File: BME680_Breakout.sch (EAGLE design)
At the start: 8 parts, among them U1 BME680

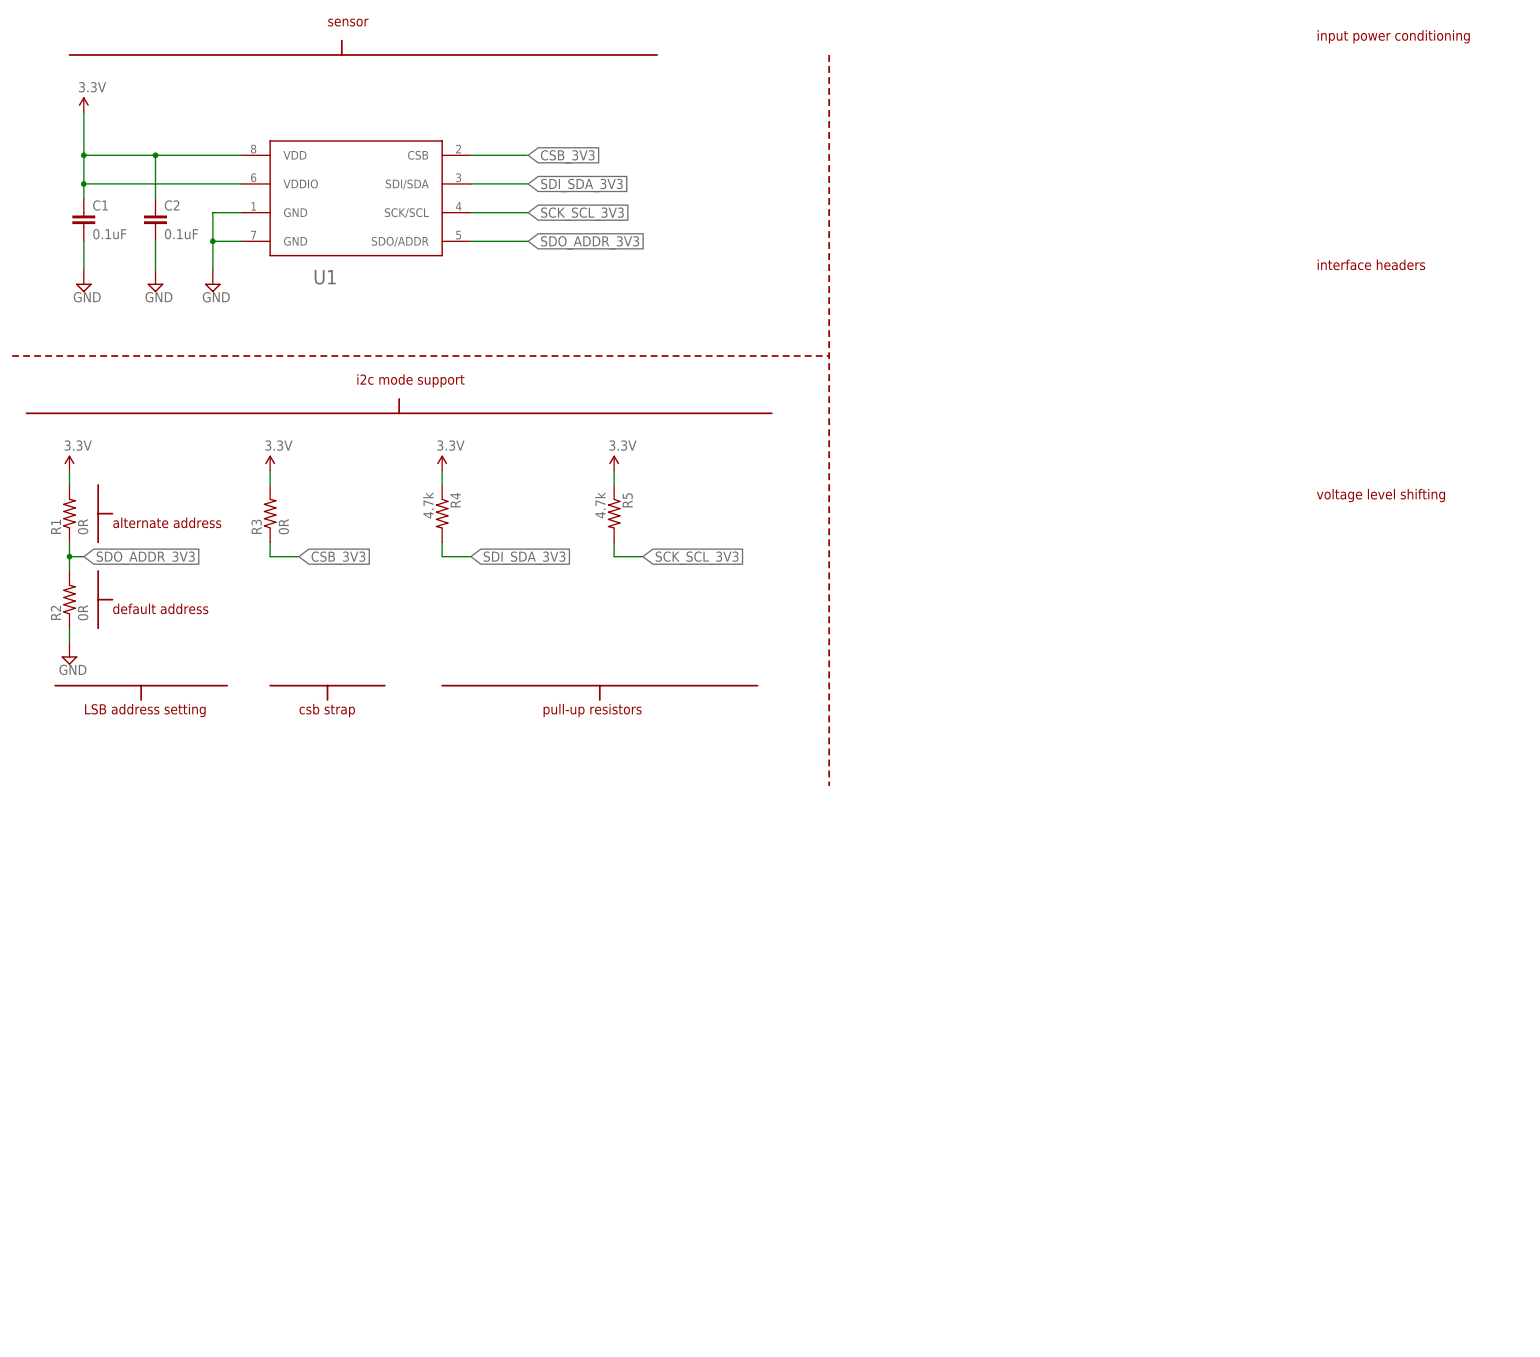
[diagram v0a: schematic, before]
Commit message: settled on i2c, renamed some signals, added level shifter logic
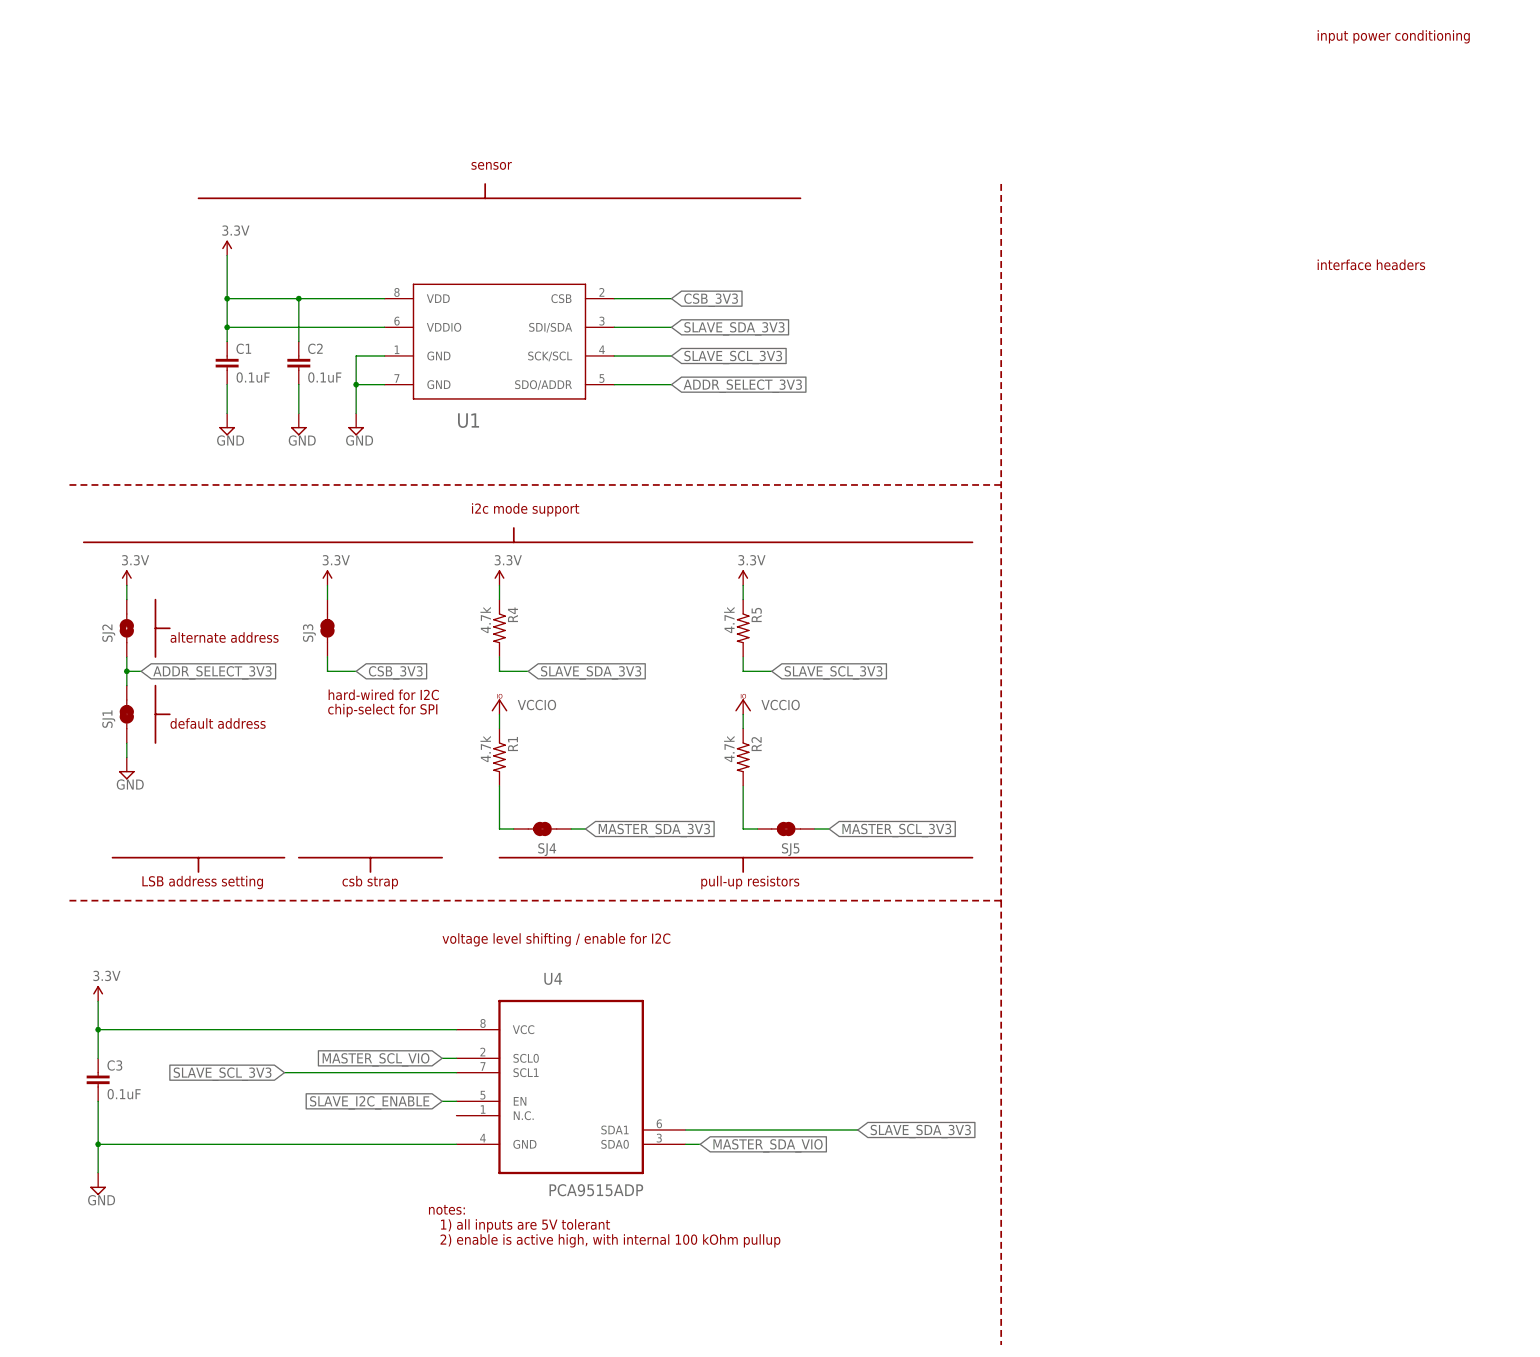
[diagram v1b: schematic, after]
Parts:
- removed R3: 0R, SparkFun-Passives:RESISTOR0805-RES
- added C3: 0.1uF, SparkFun-Passives:CAP0805
- added SJ1, SJ3, SJ4, SJ5: JUMPER-PAD-2-NC_BY_TRACE, SparkFun-Passives:JUMPER-PAD-2-NC_BY_TRACE
- added SJ2: JUMPER-PAD-2-NOYES_SILK, SparkFun-Passives:JUMPER-PAD-2-NOYES_SILK
- added U4: PCA9515ADP, PCA9515ADP:PCA9515ADP
- R1, R2: value 0R -> 4.7k
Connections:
- removed net SCK_SCL_3V3: R5.2, U1.SCK/SCL
- removed net SDI_SDA_3V3: R4.2, U1.SDI/SDA
- removed net SDO_ADDR_3V3: R1.1, R2.2, U1.SDO/ADDR
- new net ADDR_SELECT_3V3: SJ1.2, SJ2.1, U1.SDO/ADDR
- new net MASTER_SCL_3V3: SJ5.1
- new net MASTER_SCL_VIO: U4.SCL0
- new net MASTER_SDA_3V3: SJ4.1
- new net MASTER_SDA_VIO: U4.SDA0
- new net N$1: R1.2, SJ4.2
- new net N$2: R2.2, SJ5.2
- new net SLAVE_I2C_ENABLE: U4.EN
- new net SLAVE_SCL_3V3: R5.2, U1.SCK/SCL, U4.SCL1
- new net SLAVE_SDA_3V3: R4.2, U1.SDI/SDA, U4.SDA1
- new net VCCIO: R1.1, R2.1
- net 3.3V: now also C3.1, SJ2.2, SJ3.2, U4.VCC; no longer R1.2, R3.2
- net CSB_3V3: now also SJ3.1; no longer R3.1
- net GND: now also C3.2, SJ1.1, U4.GND; no longer R2.1
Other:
- note added: "chip-select for SPI"
- note added: "hard-wired for I2C"
- note added: "notes: 1) all inputs are 5V tolerant 2) enable is active high, with internal 100 kOhm pullup"
- note added: "voltage level shifting / enable for I2C"
- note removed: "voltage level shifting"
- moved on the sheet: C1, C2, R1, R2, R4, R5, U1

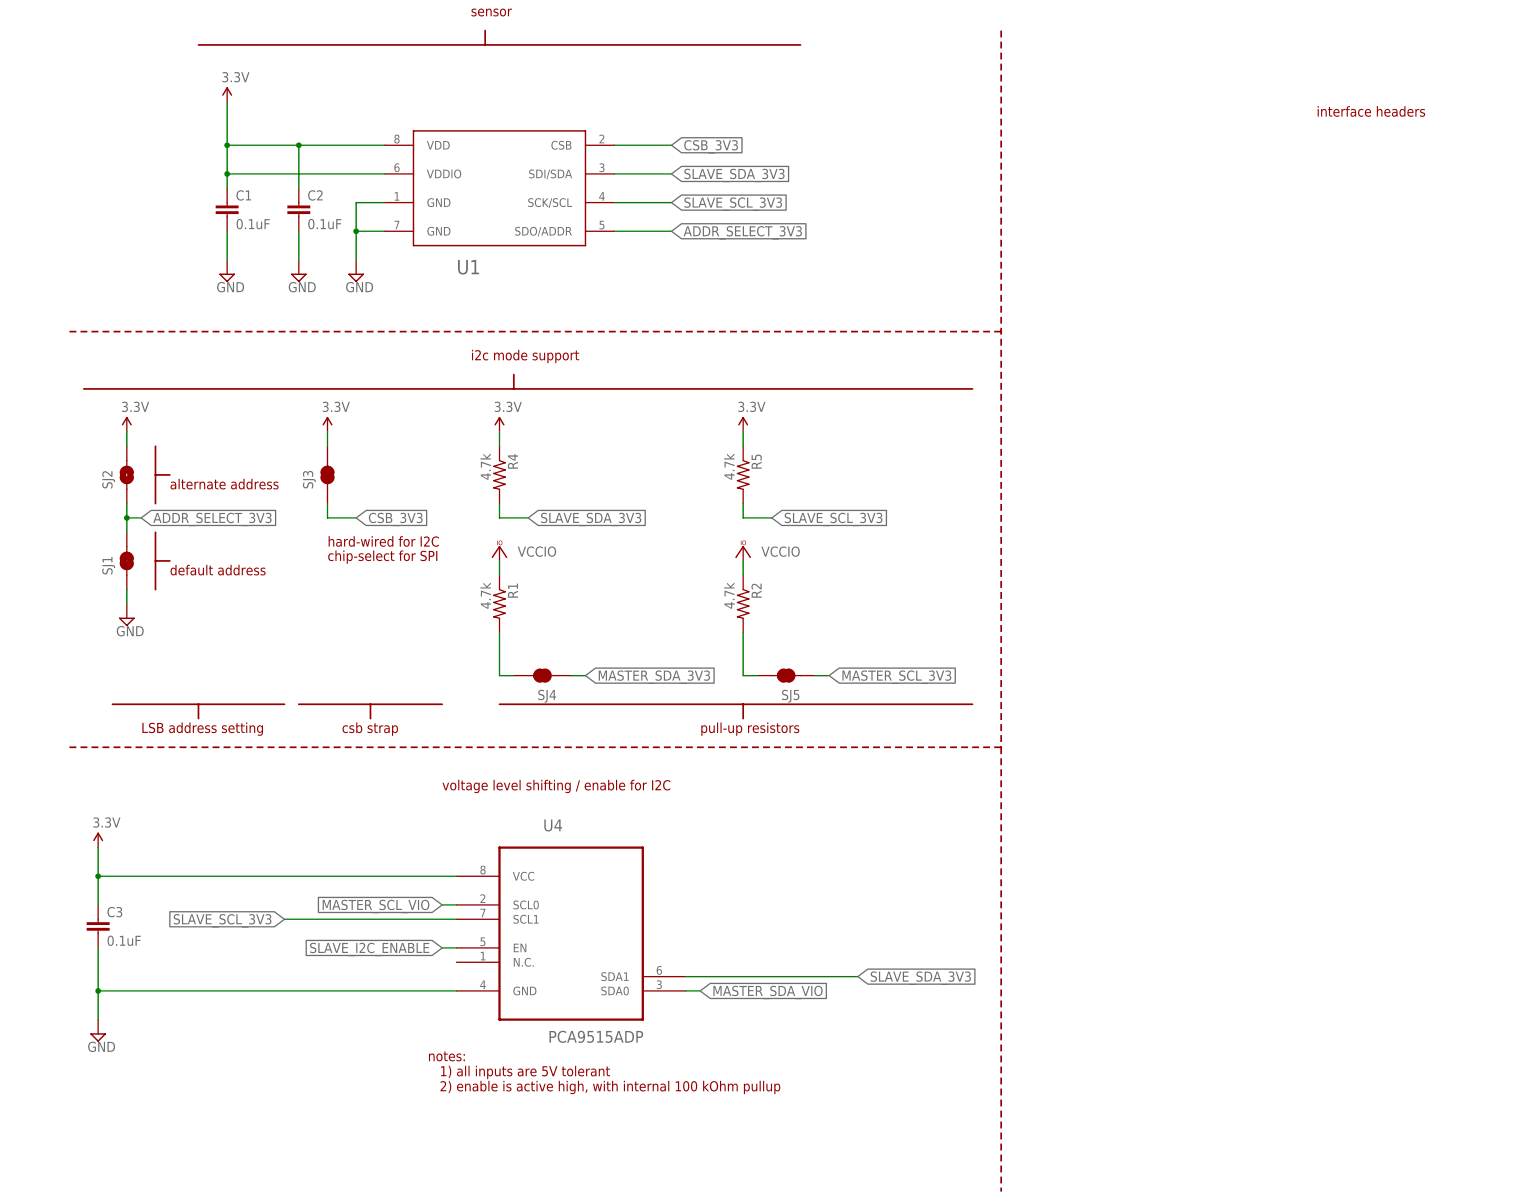
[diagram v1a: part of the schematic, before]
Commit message: added some support for SPI and wired an 8-pin interface header
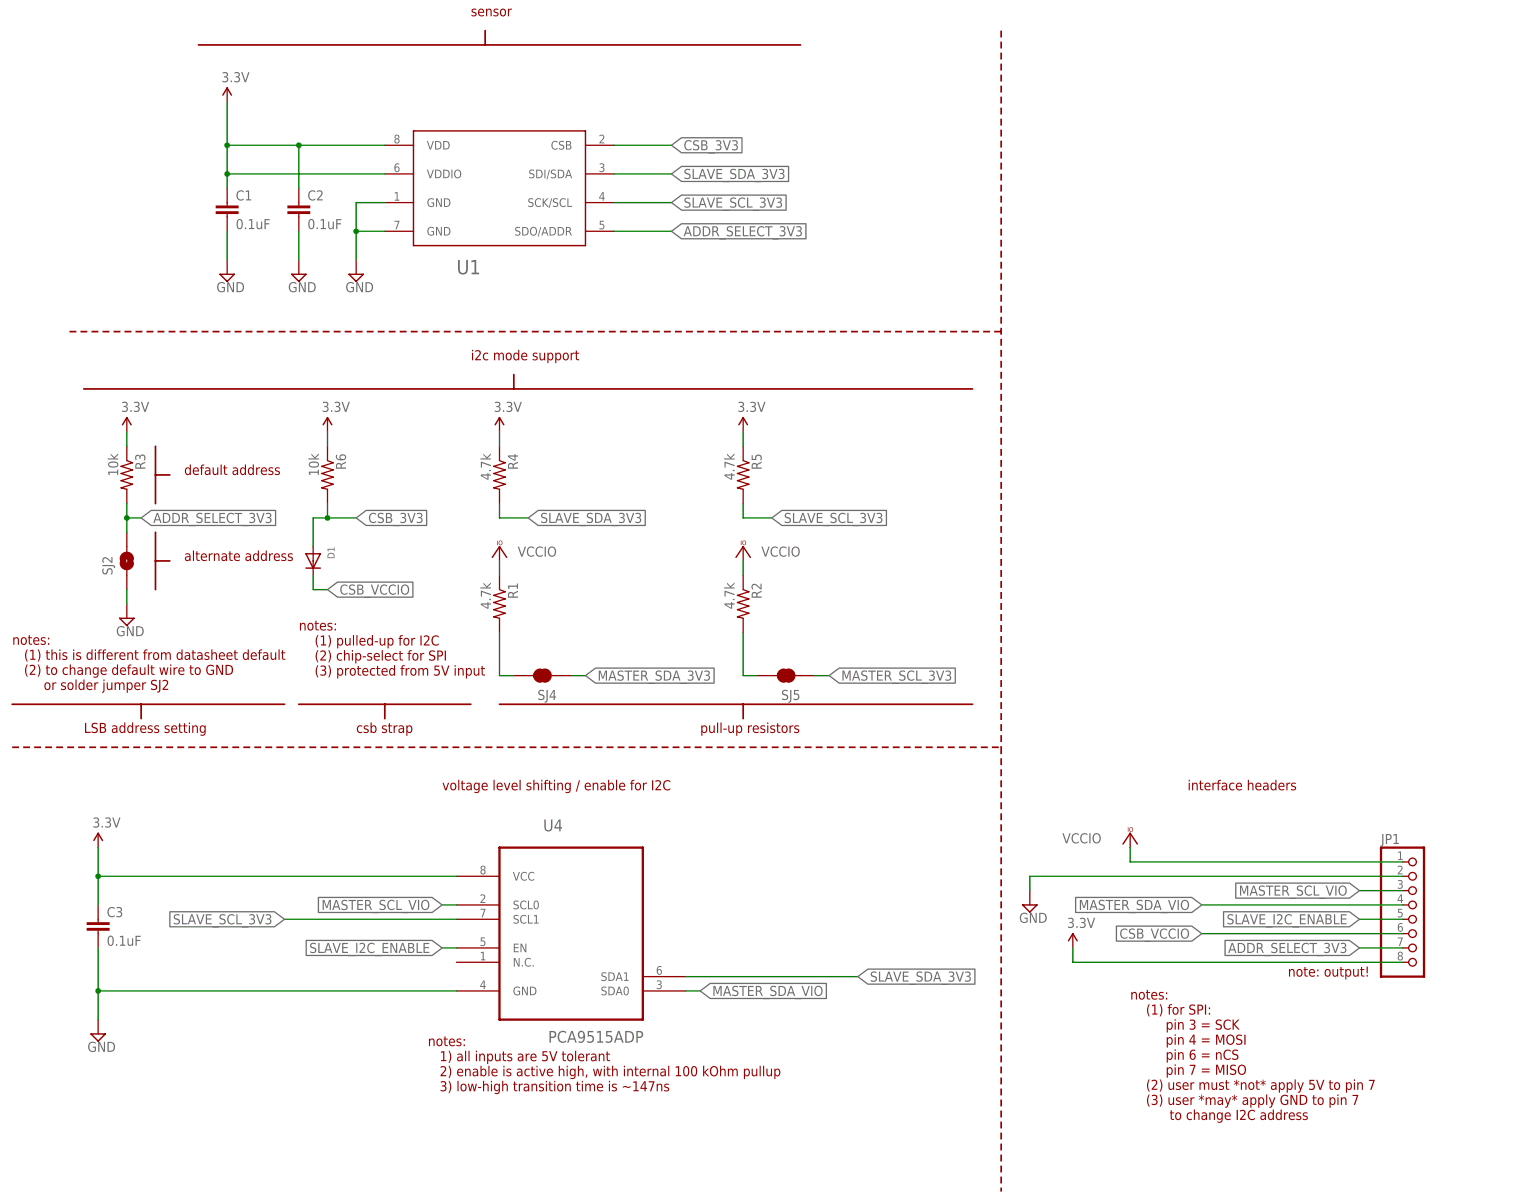
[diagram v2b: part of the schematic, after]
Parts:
- removed SJ1, SJ3: JUMPER-PAD-2-NC_BY_TRACE, SparkFun-Passives:JUMPER-PAD-2-NC_BY_TRACE
- added D1: (no value), adafruit:DIODESOD-323F
- added JP1: (no value), pinhead:PINHD-1X8
- added R3, R6: 10k, SparkFun-Passives:RESISTOR0805-RES
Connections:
- new net CSB_VCCIO: D1.C, JP1.6
- net 3.3V: now also JP1.8, R3.1, R6.1; no longer SJ2.2, SJ3.2
- net ADDR_SELECT_3V3: now also JP1.7, R3.2, SJ2.2; no longer SJ1.2, SJ2.1
- net CSB_3V3: now also D1.A, R6.2; no longer SJ3.1
- net GND: now also JP1.2, SJ2.1; no longer SJ1.1
- net MASTER_SCL_VIO: now also JP1.3
- net MASTER_SDA_VIO: now also JP1.4
- net SLAVE_I2C_ENABLE: now also JP1.5
- net VCCIO: now also JP1.1
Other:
- note added: "note: output!"
- note added: "notes: (1) for SPI: pin 3 = SCK pin 4 = MOSI pin 6 = nCS pin 7 = MISO (2) user must *not* apply 5V to pin 7 (3) user *may* apply GND to pin 7 to change I2C address"
- note added: "notes: (1) pulled-up for I2C (2) chip-select for SPI (3) protected from 5V input"
- note added: "notes: (1) this is different from datasheet default (2) to change default wire to GND or solder jumper SJ2"
- note added: "notes: 1) all inputs are 5V tolerant 2) enable is active high, with internal 100 kOhm pullup 3) low-high transition time is ~147ns"
- note removed: "chip-select for SPI"
- note removed: "hard-wired for I2C"
- note removed: "notes: 1) all inputs are 5V tolerant 2) enable is active high, with internal 100 kOhm pullup"
- moved on the sheet: SJ2

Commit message: added input power regulator, still need bypass solution, reorganized schematic slightly
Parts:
- added C4, C5: 10uF, SparkFun-Passives:CAP0805
- added U8: LD1117XX, wicked-device:LD1117XX
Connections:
- net 3.3V: now also C5.1, U8.VO
- net GND: now also C4.2, C5.2, U8.GND
- net VCCIO: now also C4.1, U8.VI
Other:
- note added: "note: cut jumper for external pull-up"
- note added: "notes: (1) for SPI: pin 3 = SCK pin 4 = MOSI pin 6 = nCS pin 7 = MISO (2) user must *never* apply 5V to pin 7 (3) user *may* apply GND to pin 7 to change I2C address"
- note added: "notes: (1) this only works for 5v input (2) need a way to bypass it for 3.3v input"
- note removed: "notes: (1) for SPI: pin 3 = SCK pin 4 = MOSI pin 6 = nCS pin 7 = MISO (2) user must *not* apply 5V to pin 7 (3) user *may* apply GND to pin 7 to change I2C address"
- moved on the sheet: C1, C2, C3, D1, JP1, R1, R2, R3, R4, R5, R6, SJ2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
